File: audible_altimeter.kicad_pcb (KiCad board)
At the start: 2 copper layers, 52 x 29 mm, 54 parts, among them CON1 BUQ2-USB-MICRO-B, IC1 BUQ2-ATXMEGA128A4U-A, P1 CONN_2, P2 SERIAL, Q1 NPN-SOT23, U1 MCP7940M, U10 CNT, U11 DWN, U12 2SMPB-01-01, U13 FLASH_MEMORY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

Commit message: Before starting laying out tracks
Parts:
- added C10: 100n, buq2:SM0603, F.Cu at (179.4, 123.0)
- added P3: POWER, buq2:PIN_HEADER_2, F.Cu at (180.8, 111.2)
- added R9: 10k, buq2:SM0603, F.Cu at (177.3, 123.0)
- added U15: SPDT-SWITCH, buq2:CUS-12TB-SWITCH, F.Cu at (137.5, 120.6)
- added U16: MPU-9250, buq2:24QFN-3MM-3MM, F.Cu at (183.5, 121.5)
- added XC13: 10n, buq2:SM0603, F.Cu at (185.7, 119.0)
- added XC14: 100n, buq2:SM0603, F.Cu at (181.5, 123.0)
- moved P2 34.8 mm to (183.7, 111.2), turned to 90 degrees
- moved U8 13.9 mm to (182.9, 101.6)
- moved R7 12.3 mm to (169.2, 103.4), turned to 90 degrees
- moved R8 10.9 mm to (166.7, 103.1), turned to 90 degrees
- moved U14 8.98 mm to (165.6, 98.9)
- moved U9 7.37 mm to (185.8, 111.6)
- moved R6 7.31 mm to (155.7, 122.8)
- moved C7 7.30 mm to (161.0, 122.8)
- moved R5 7.11 mm to (157.9, 122.8)
- moved U12 6.90 mm to (164.6, 122.7)
- moved C8 6.80 mm to (167.8, 122.7)
- moved Q1 6.15 mm to (166.7, 107.6)
- moved XC5 5.23 mm to (180.8, 114.3)
- moved D2 5.19 mm to (170.1, 98.8)
- moved R1 4.88 mm to (170.6, 112.5), turned to 90 degrees
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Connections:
- net /Barometer/I2C_SCL renamed /Accelerometer/I2C_SCL
- net /Barometer/I2C_SDA renamed /Accelerometer/I2C_SDA
- IC1 pad 24: (no net) -> /Buzzer/BUZZER_DRIVE
- IC1 pad 40: (no net) -> /Battery/+3.3V
- IC1 pad 5: (no net) -> /MCU/ACC_INT
- P1 pad 2: /Battery/BATTERY -> /Battery/BATTERY-DIRECT
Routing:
- net /Battery/BATTERY: track 0.00 -> 26.9 mm
- net /Battery/BATTERY-DIRECT: track 0.00 -> 4.54 mm
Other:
- outline, holes or cut-outs redrawn
- board text added: "AudibleA V3.0 Matti Jukola 2015-04-17"
- board text removed: "AudibleA V2.0 Matti Jukola 2015-01-27"

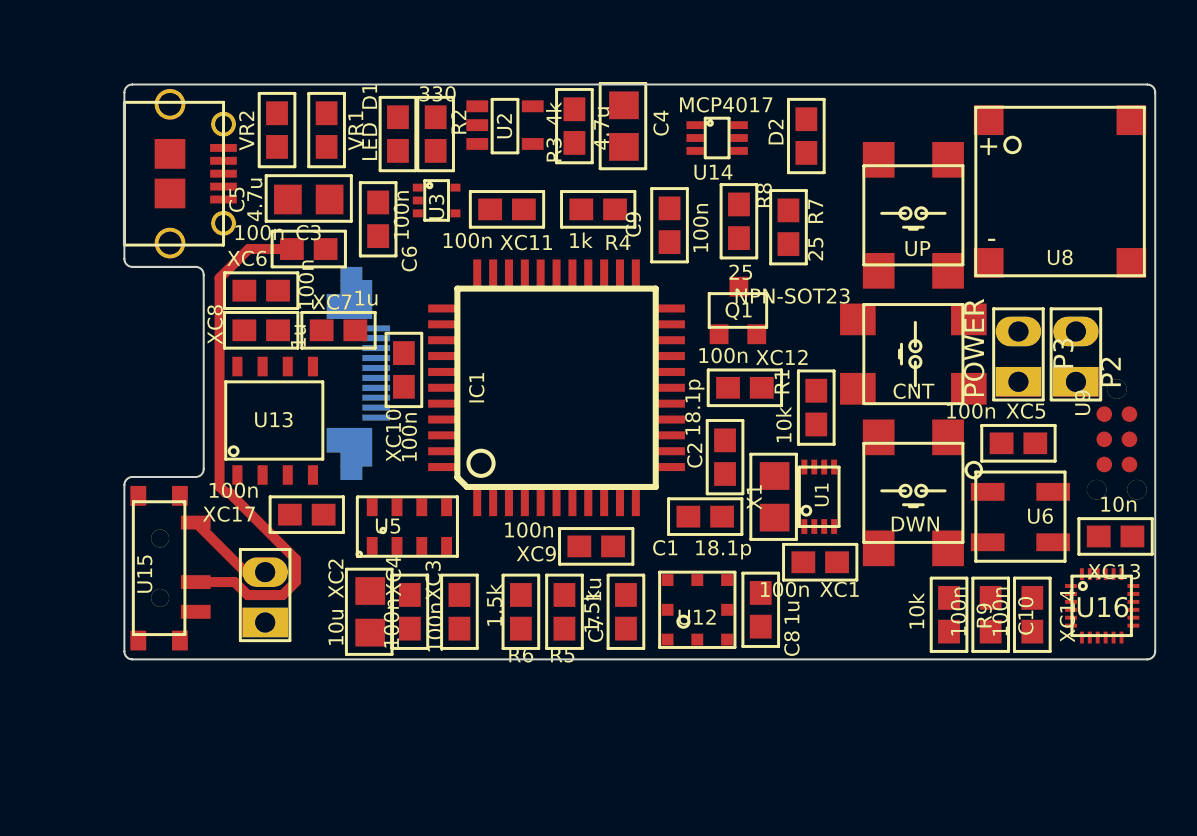
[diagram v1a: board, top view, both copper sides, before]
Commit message: Continuing laying out tracks
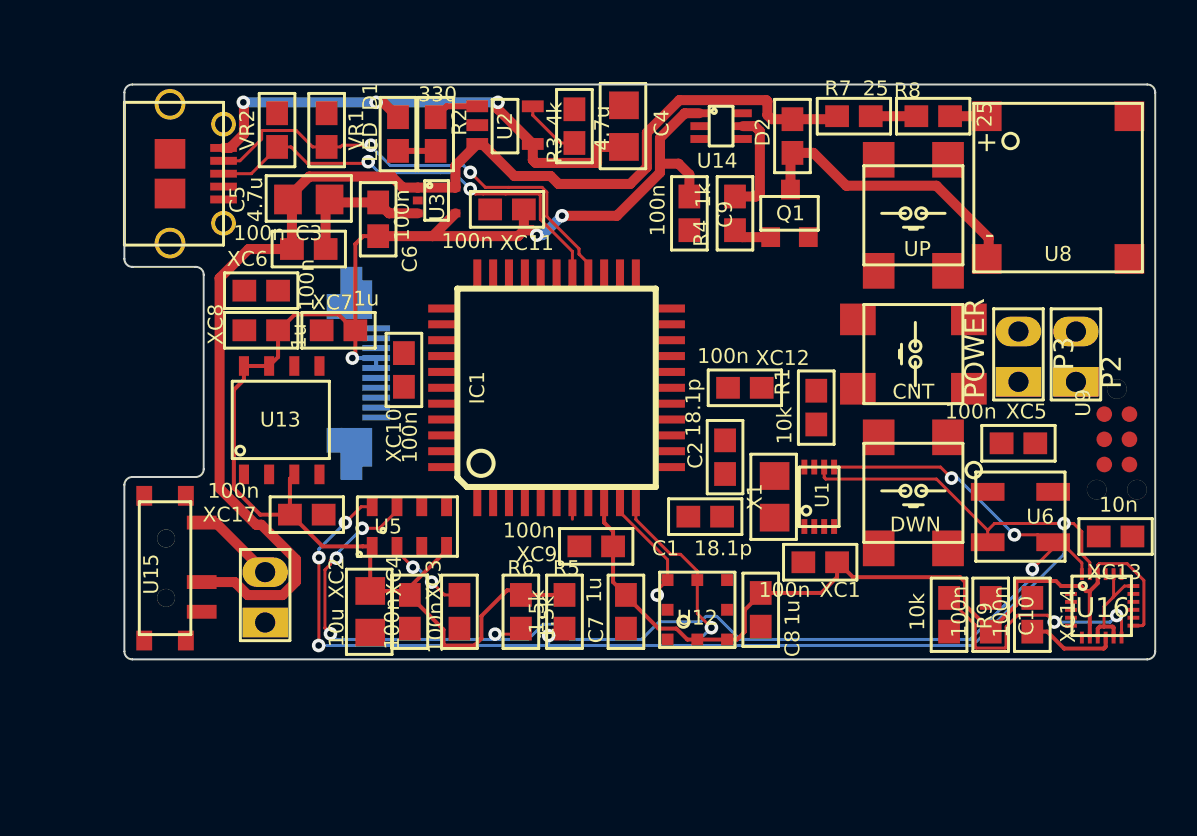
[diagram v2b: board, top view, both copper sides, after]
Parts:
- U8: value SPEAKER-WITH-DUMMY -> CSS-0575A-SMT
- moved R8 11.1 mm to (176.5, 97.8), turned to 180 degrees
- moved R4 6.90 mm to (166.5, 102.7), turned to 90 degrees
- moved R7 6.50 mm to (172.5, 97.8), turned to 180 degrees
- moved Q1 5.55 mm to (169.3, 102.7)
- moved C9 1.17 mm to (164.2, 102.7), turned to 90 degrees
- moved D2 0.70 mm to (169.4, 98.8)
- moved U14 0.63 mm to (165.8, 98.3)
- moved U13 0.33 mm to (141.7, 115.9)
- moved U15 0.30 mm to (137.8, 120.6)
- moved U8 0.22 mm to (182.8, 101.4)
- turned R5 to 270 degrees
- turned R6 to 270 degrees
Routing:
- net /Battery/+3.3V: track 0.00 -> 123.1 mm, vias 0 -> 3
- net /Accelerometer/I2C_SCL: track 0.00 -> 79.2 mm, vias 0 -> 6
- net /Accelerometer/I2C_SDA: track 0.00 -> 73.8 mm, vias 0 -> 8
- net /Battery/BATTERY: track 26.9 -> 63.7 mm
- net /Battery/+5V: track 0.00 -> 26.5 mm, vias 0 -> 3
- net /MCU/D-: track 0.00 -> 23.6 mm, vias 0 -> 2
- net /MCU/D+: track 0.00 -> 22.3 mm, vias 0 -> 2
- net Net-(D2-Pad1): track 0.00 -> 14.8 mm
- net GND: track 0.00 -> 13.3 mm
- net /MCU/ACC_INT: track 0.00 -> 13.0 mm, vias 0 -> 2
- net Net-(R4-Pad2): track 0.00 -> 5.40 mm
- net Net-(U16-Pad10): track 0.00 -> 4.55 mm
- net Net-(U5-Pad2): track 0.00 -> 4.51 mm, vias 0 -> 2
- net Net-(R3-Pad1): track 0.00 -> 3.13 mm
- net Net-(R2-Pad2): track 0.00 -> 2.33 mm
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
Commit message: Ordered v3.0
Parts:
- moved U6 0.40 mm to (181.3, 118.0)
- moved XC13 0.10 mm to (185.8, 119.0)
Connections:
- IC1 pad 1: /Buttons/BUTTON_DOWN -> (no net)
- IC1 pad 2: /Buttons/BUTTON_CENTER -> (no net)
- IC1 pad 20: (no net) -> /Buttons/BUTTON_DOWN
- IC1 pad 21: (no net) -> /Buttons/BUTTON_CENTER
- IC1 pad 22: (no net) -> /Buttons/BUTTON_UP
- IC1 pad 3: /Buttons/BUTTON_UP -> (no net)
- IC1 pad 32: Net-(IC1-Pad32) -> /MCU/RX
- IC1 pad 33: Net-(IC1-Pad33) -> /MCU/TX
- P2 pad 1: Net-(IC1-Pad33) -> /MCU/RX
- P2 pad 2: Net-(IC1-Pad32) -> /MCU/TX
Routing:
- net /Battery/+3.3V: track 123.1 -> 209.1 mm, vias 3 -> 10
- net GND: track 13.3 -> 89.1 mm, vias 0 -> 40
- net /Accelerometer/I2C_SDA: track 73.8 -> 117.8 mm, vias 8 -> 9
- net /Accelerometer/I2C_SCL: track 79.2 -> 122.5 mm, vias 6 -> 12
- net /MCU/RX: track 0.00 -> 42.1 mm, vias 0 -> 2
- net /MCU/TX: track 0.00 -> 38.3 mm, vias 0 -> 2
- net /MCU/PDI_CLK: track 0.00 -> 37.1 mm, vias 0 -> 6
- net /MCU/PDI_DATA: track 0.00 -> 36.6 mm, vias 0 -> 4
- net /MCU/SCK: track 0.00 -> 29.8 mm, vias 0 -> 2
- net /Display/MOSI: track 0.00 -> 26.7 mm, vias 0 -> 1
- net /MCU/ACC_INT: track 13.0 -> 36.9 mm, vias 2 -> 6
- net /MCU/MISO: track 0.00 -> 23.8 mm, vias 0 -> 2
- net /MCU/CLOCK_INT: track 0.00 -> 22.8 mm, vias 0 -> 2
- net /Buttons/BUTTON_DOWN: track 0.00 -> 21.8 mm, vias 0 -> 2
- net /Buzzer/BUZZER_DRIVE: track 0.00 -> 17.3 mm
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- added copper zone on B.Cu, net GND
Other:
- board text added: "+"
- board text added: "3.3V"
- board text added: "AudibleA V3.0 Matti Jukola 2015-04-18"
- board text added: "BTR"
- board text added: "GND"
- board text removed: "AudibleA V3.0 Matti Jukola 2015-04-17"

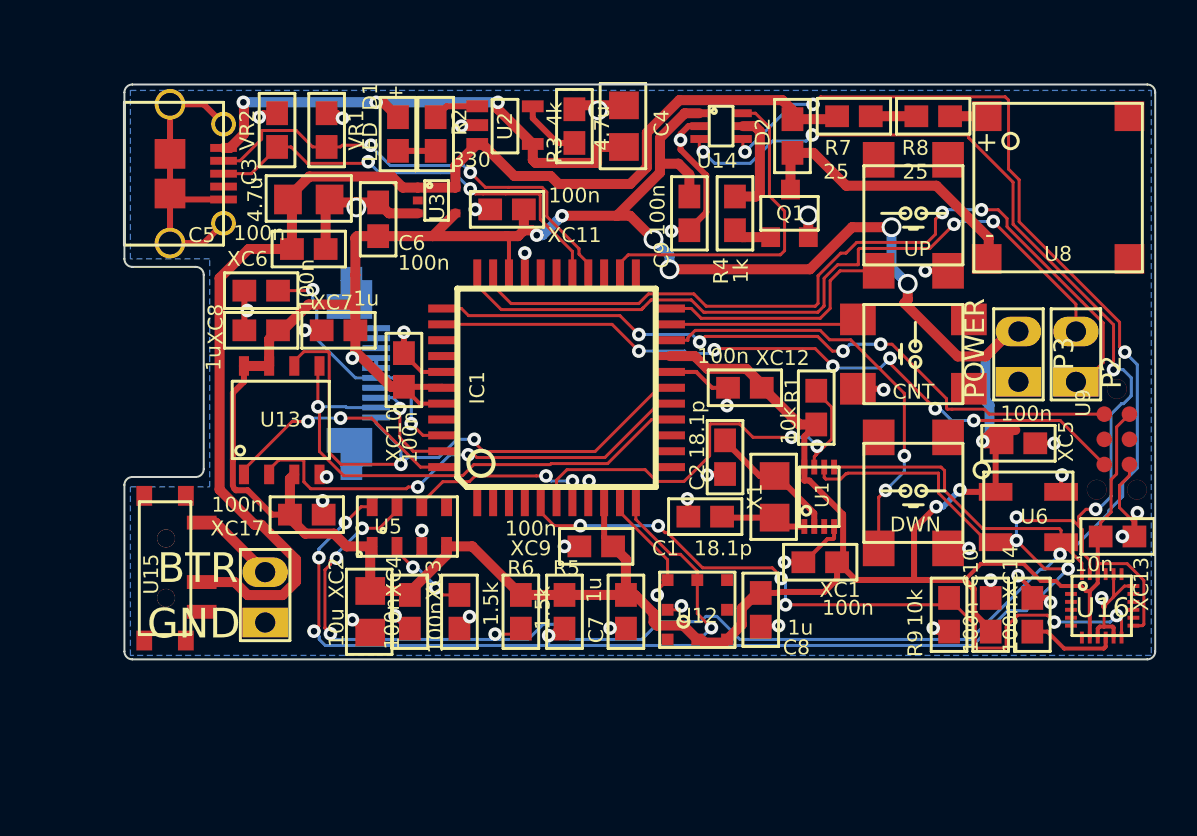
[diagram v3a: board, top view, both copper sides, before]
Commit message: Change few footprints to ones with (simple) 3d models
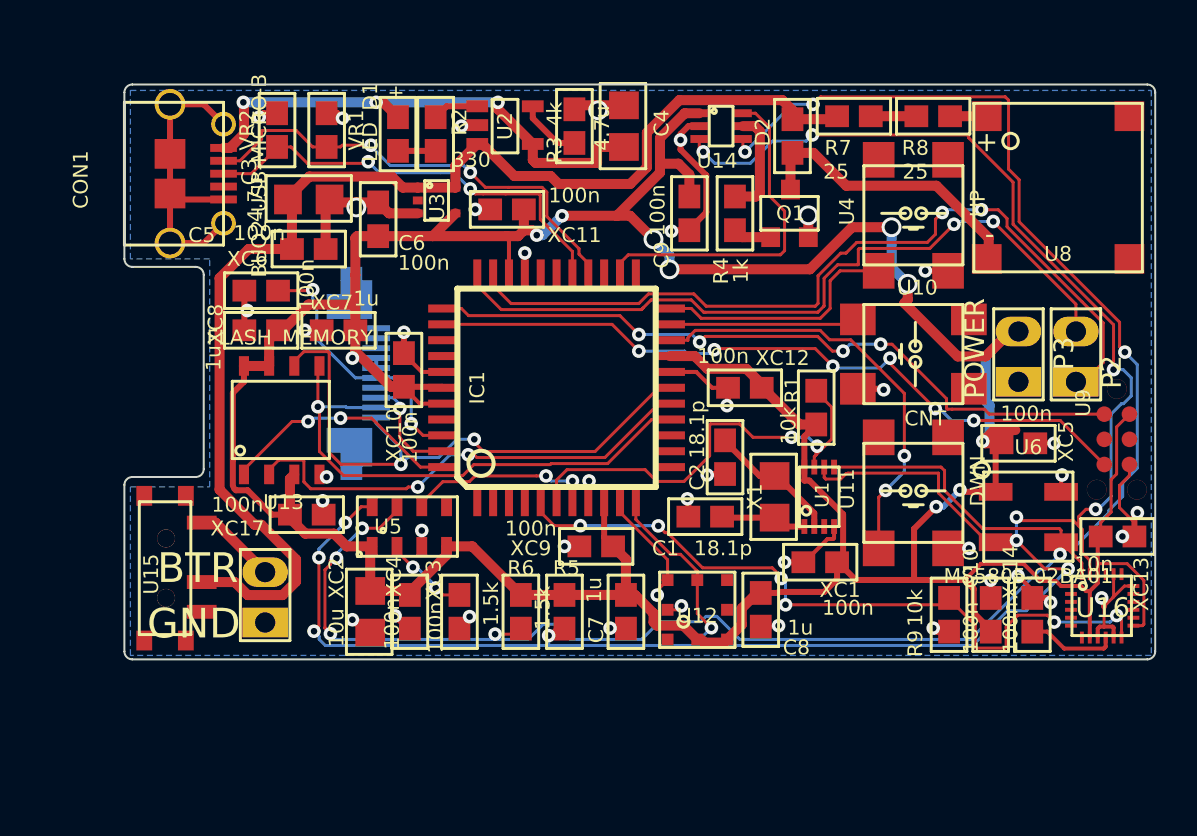
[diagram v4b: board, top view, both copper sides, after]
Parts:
- moved U13 3.34 mm to (143.6, 113.1)

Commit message: Some changes?
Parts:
- removed C10, XC14, XC5: 100n, buq2:SM0603
- removed C7, C8: 1u, buq2:SM0603
- removed U12: 2SMPB-01-01, buq2:2SMPB-01-01
- removed U16: MPU-9250, buq2:24QFN-3MM-3MM
- removed U6: MS5805-02BA01, buq2:MS5805-02BA01
- removed XC13: 10n, buq2:SM0603
- R9: value 10k -> 500k
- moved R9 7.90 mm to (173.2, 129.7)
- moved CON1 1.30 mm to (139.4, 100.7)
- moved U15 0.50 mm to (137.3, 120.6)
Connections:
- net /Accelerometer/I2C_SCL renamed /Barometer/I2C_SCL
- net /Accelerometer/I2C_SDA renamed /Barometer/I2C_SDA
- IC1 pad 41: (no net) -> /Battery/BATTERY_SENSE
- IC1 pad 5: /MCU/ACC_INT -> (no net)
- R9 pad 1: GND -> /Battery/BATTERY
- R9 pad 2: /MCU/ACC_INT -> /Battery/BATTERY_SENSE
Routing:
- net /MCU/ACC_INT: track 36.9 -> 0.00 mm, vias 6 -> 0
- net GND: track 89.1 -> 67.7 mm, vias 40 -> 28
- net (no net): track 0.00 -> 17.4 mm, vias 0 -> 6
- net /Battery/+3.3V: track 209.1 -> 198.1 mm
- net Net-(U16-Pad10): track 4.55 -> 0.00 mm
- net /Barometer/I2C_SCL: track 122.5 -> 119.9 mm
- net /Barometer/I2C_SDA: track 117.8 -> 115.5 mm
- net /MCU/D-: track 23.6 -> 24.9 mm
- net /MCU/D+: track 22.3 -> 23.6 mm
- net /Battery/+5V: track 26.5 -> 27.8 mm
- removed copper zone on B.Cu, net GND
